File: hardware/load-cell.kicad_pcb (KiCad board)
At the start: 2 copper layers, 30 x 30 mm, 36 parts, among them P1 CON-SENSOR, P2 Boot, P3 Debug, P4 AKL_5_2, P5 AKL_5_2, U1 XMC1XXX24, U2 FAN4860, U3 HX711, U4 DRILL, U5 DRILL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

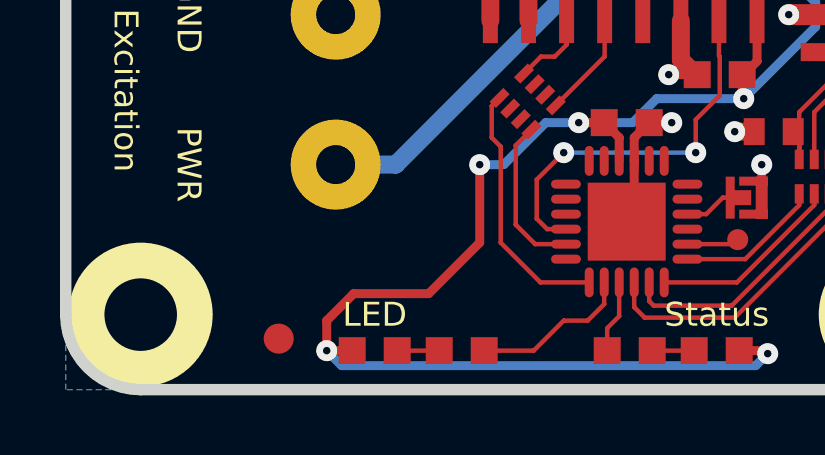
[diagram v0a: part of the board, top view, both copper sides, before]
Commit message: rename LED
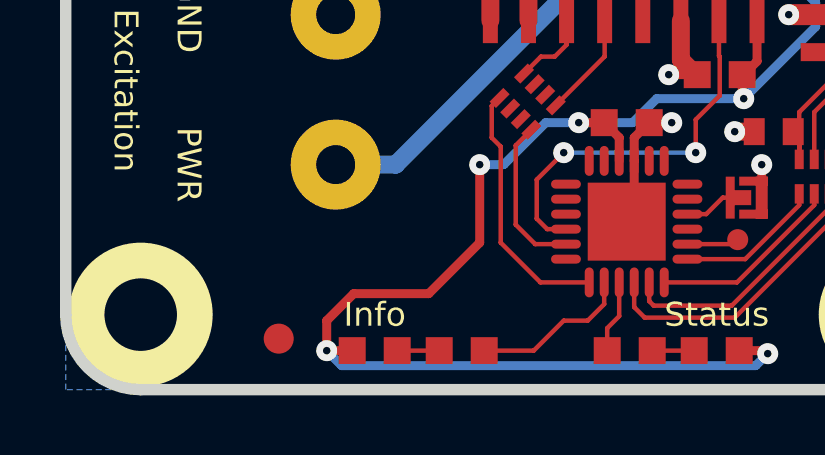
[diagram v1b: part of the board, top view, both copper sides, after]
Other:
- board text added: "Info"
- board text removed: "LED"
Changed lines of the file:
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@@
     (effects (font (size 0.8001 0.8001) (thickness 0.14986)))
   )
-  (gr_text LED (at 148.35 112.575) (layer F.SilkS)
+  (gr_text Info (at 148.35 112.575) (layer F.SilkS)
     (effects (font (size 0.8001 0.8001) (thickness 0.14986)))
   )

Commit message: specify processor
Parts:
- U1: value XMC1XXX24 -> XMC1100
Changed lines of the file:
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@@
       (effects (font (size 0.3 0.3) (thickness 0.075)))
     )
-    (fp_text value XMC1XXX24 (at 0 0.8 180) (layer F.Fab)
+    (fp_text value XMC1100 (at 0 0.8 180) (layer F.Fab)
       (effects (font (size 0.3 0.3) (thickness 0.075)))
     )
